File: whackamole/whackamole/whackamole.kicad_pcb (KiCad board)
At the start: 2 copper layers, 61 x 43.2 mm, 20 parts, among them Q1 PN2222A, U1 PC817

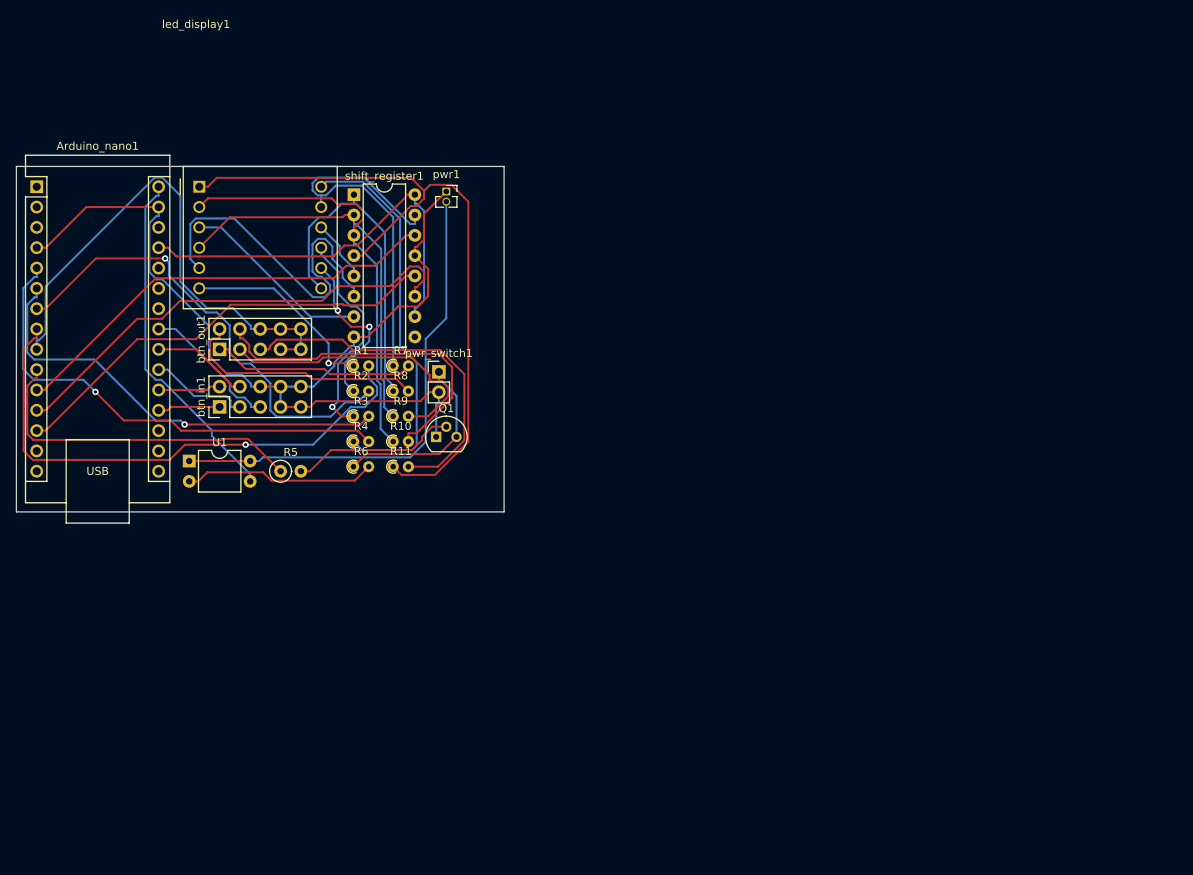
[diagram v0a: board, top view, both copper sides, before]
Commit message: capacitor to regulate player tension and avoid unexpected shutdowns
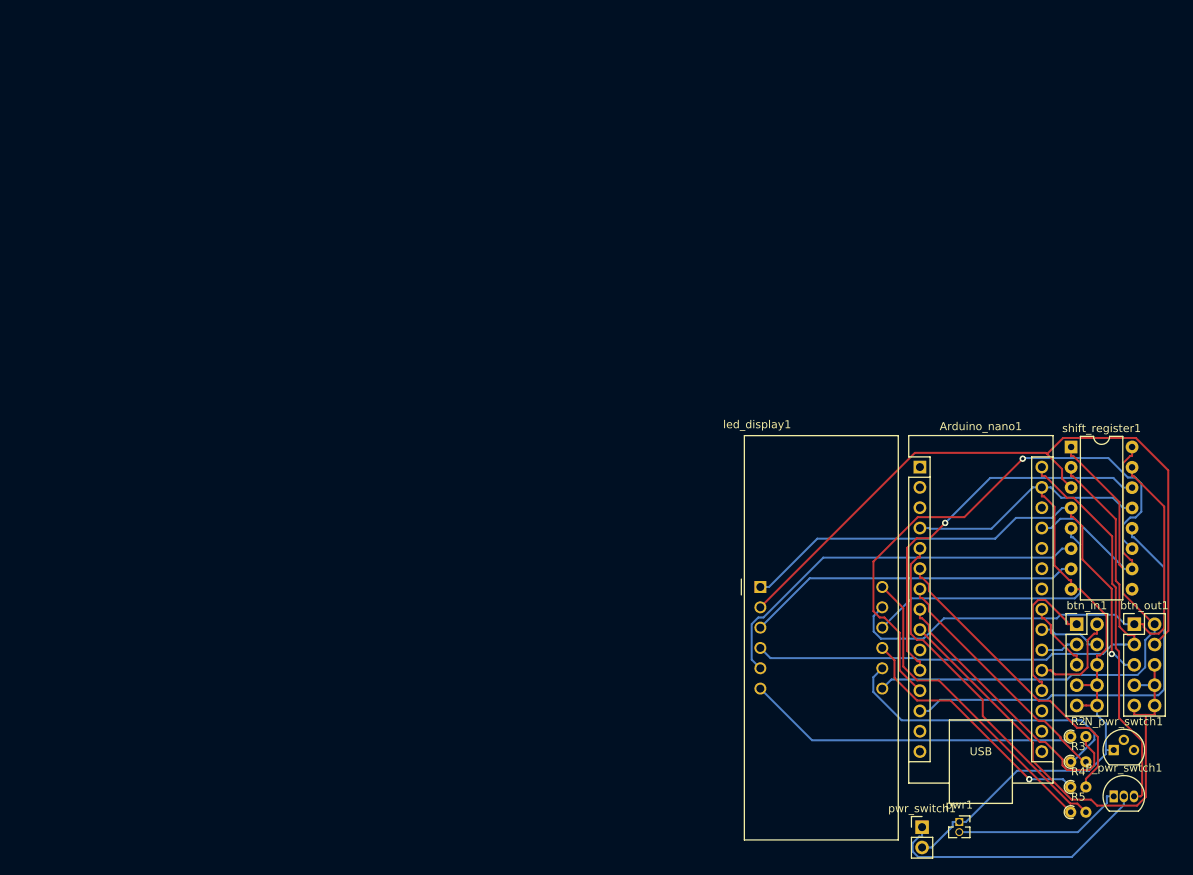
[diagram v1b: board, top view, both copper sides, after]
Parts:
- removed Q1: PN2222A, Package_TO_SOT_THT:TO-92
- removed R1, R10, R11, R7, R8, R9: 220, Resistor_THT:R_Axial_DIN0204_L3.6mm_D1.6mm_P1.90mm_Vertical
- removed R6: 330, Resistor_THT:R_Axial_DIN0204_L3.6mm_D1.6mm_P1.90mm_Vertical
- removed U1: PC817, Package_DIP:DIP-4_W7.62mm
- added N_pwr_swtch1: 512-BS270, Package_TO_SOT_THT:TO-92, F.Cu at (162.6, 90.7)
- added P_pwr_swtch1: VP3203N3-G, Package_TO_SOT_THT:TO-92_Inline, F.Cu at (162.6, 96.5)
- R2, R3, R4: value 220 -> 470
- R5: value 10k -> 470; footprint Resistor_THT:R_Axial_DIN0207_L6.3mm_D2.5mm_P2.54mm_Vertical -> Resistor_THT:R_Axial_DIN0204_L3.6mm_D1.6mm_P1.90mm_Vertical
- moved btn_out1 119.4 mm to (165.1, 75.0), turned to 0 degrees
- moved Arduino_nano1 115.8 mm to (138.3, 55.4)
- moved btn_in1 110.5 mm to (157.9, 75.0), turned to 0 degrees
- moved R5 107.6 mm to (157.2, 98.5)
- moved pwr1 101.6 mm to (143.3, 99.7)
- moved R2 99.5 mm to (157.2, 89.0)
- moved R3 99.5 mm to (157.2, 92.2)
- moved R4 99.5 mm to (157.2, 95.3)
- moved shift_register1 95.0 mm to (157.2, 52.9)
- moved led_display1 86.2 mm to (118.4, 70.3)
- moved pwr_switch1 83.0 mm to (138.6, 100.4)
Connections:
- Arduino_nano1 pad 14: unconnected-(Arduino_nano1-MOSI-Pad14) -> Net-(Arduino_nano1-MOSI)
- Arduino_nano1 pad 15: unconnected-(Arduino_nano1-MISO-Pad15) -> Net-(Arduino_nano1-MISO)
- R2 pad 1: Net-(led_display1-CA3) -> Net-(led_display1-CA4)
- R2 pad 2: Net-(Arduino_nano1-D4) -> Net-(Arduino_nano1-D5)
- R3 pad 1: Net-(led_display1-CA2) -> Net-(led_display1-CA3)
- R3 pad 2: Net-(Arduino_nano1-D3) -> Net-(Arduino_nano1-D4)
- R4 pad 1: Net-(led_display1-CA1) -> Net-(led_display1-CA2)
- R4 pad 2: Net-(Arduino_nano1-D2) -> Net-(Arduino_nano1-D3)
- R5 pad 1: Net-(Arduino_nano1-D7) -> Net-(led_display1-CA1)
- R5 pad 2: Net-(Q1-B) -> Net-(Arduino_nano1-D2)
- led_display1 pad 1: Net-(led_display1-e) -> Net-(btn_out1-Pin_5)
- led_display1 pad 11: Net-(led_display1-a) -> Net-(btn_out1-Pin_1)
- led_display1 pad 2: Net-(led_display1-d) -> Net-(btn_out1-Pin_4)
- led_display1 pad 4: Net-(led_display1-c) -> Net-(btn_out1-Pin_3)
- led_display1 pad 7: Net-(led_display1-b) -> Net-(btn_out1-Pin_2)
- pwr1 pad 2: +5V -> +6V
- shift_register1 pad 1: Net-(led_display1-b) -> Net-(btn_out1-Pin_2)
- shift_register1 pad 15: Net-(led_display1-a) -> Net-(btn_out1-Pin_1)
- shift_register1 pad 2: Net-(led_display1-c) -> Net-(btn_out1-Pin_3)
- shift_register1 pad 3: Net-(led_display1-d) -> Net-(btn_out1-Pin_4)
- shift_register1 pad 4: Net-(led_display1-e) -> Net-(btn_out1-Pin_5)
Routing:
- net Net-(led_display1-e): track 90.3 -> 0.00 mm
- net +5V: track 61.7 -> 0.00 mm
- net Net-(led_display1-d): track 53.2 -> 0.00 mm
- net Net-(led_display1-a): track 50.0 -> 0.00 mm
- net Net-(led_display1-c): track 48.4 -> 0.00 mm
- net Net-(btn_out1-Pin_4): track 42.4 -> 89.5 mm
- net Net-(Arduino_nano1-D7): track 42.4 -> 0.00 mm
- net Net-(led_display1-b): track 41.9 -> 0.00 mm
- net Net-(btn_out1-Pin_1): track 25.5 -> 64.8 mm
- net Net-(btn_out1-Pin_3): track 36.0 -> 74.2 mm
- net Net-(btn_out1-Pin_2): track 31.0 -> 66.8 mm
- net Net-(Arduino_nano1-D5): track 68.1 -> 35.9 mm, vias 1 -> 0
- net Net-(Arduino_nano1-D4): track 58.6 -> 30.9 mm, vias 1 -> 0
- net Net-(led_display1-f): track 7.88 -> 35.2 mm
- net Net-(R6-Pad2): track 24.1 -> 0.00 mm
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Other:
- board outline removed
